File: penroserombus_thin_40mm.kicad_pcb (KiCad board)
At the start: 2 copper layers, 72.4 x 23.5 mm, 15 parts, among them J1 Conn_01x03_Female, J2 Conn_01x03_Female, J3 Conn_01x03_Male, J4 Conn_01x03_Male, M2 MountingHole_2.2mm_M2_ISO7380, SW1 SW_DPDT_x2

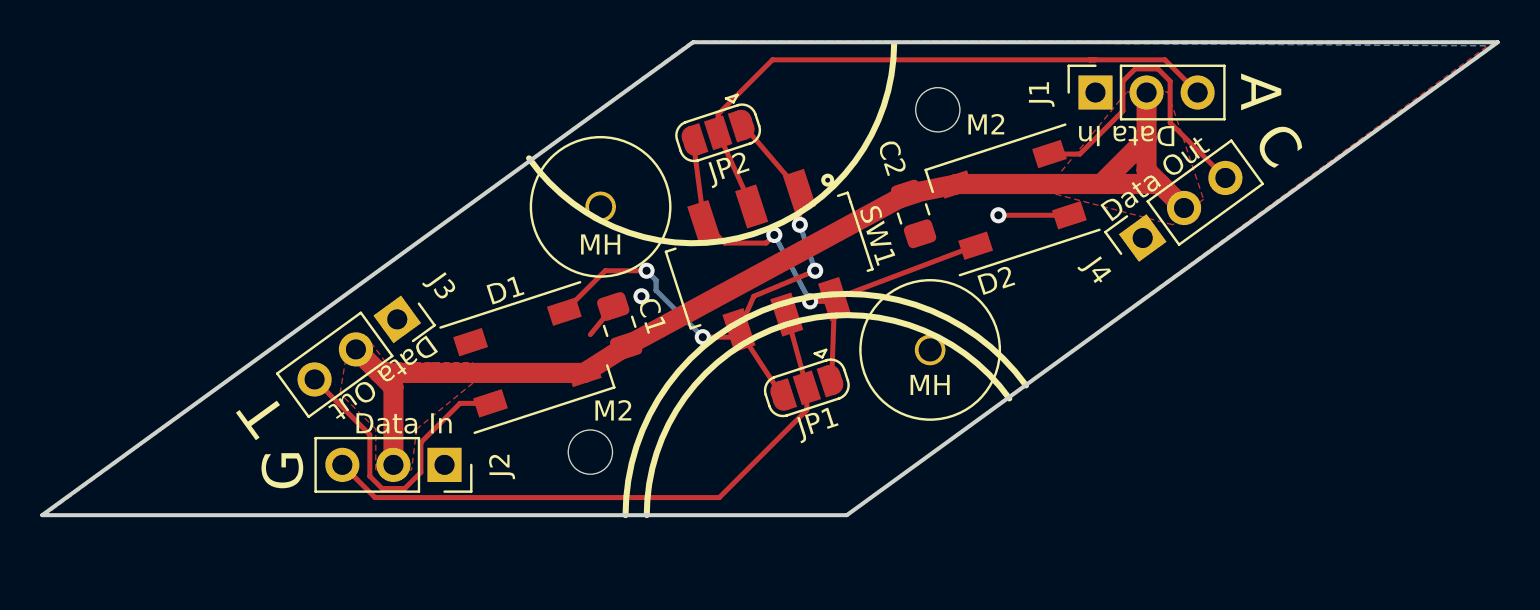
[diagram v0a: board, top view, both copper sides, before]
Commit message: made 3535 led version
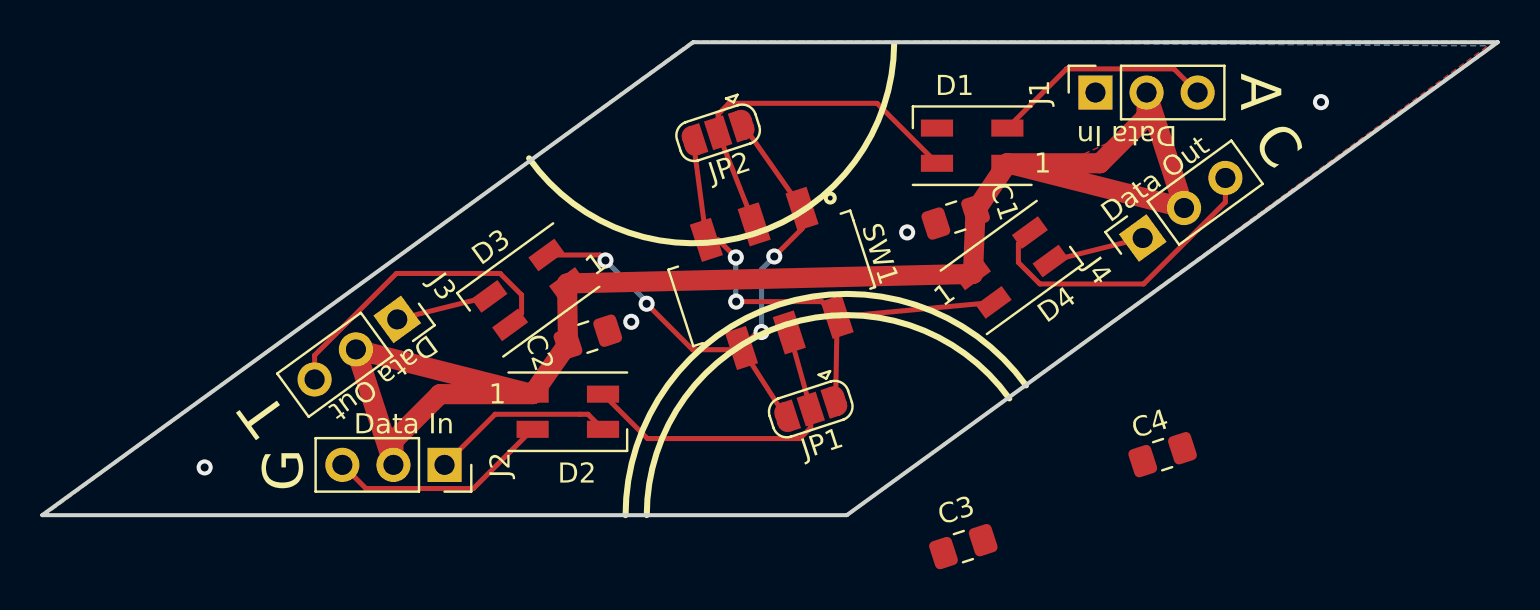
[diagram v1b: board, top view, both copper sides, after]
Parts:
- removed M2 (x2): MountingHole_2.2mm_M2_ISO7380, MountingHole:MountingHole_2.2mm_M2_ISO7380
- removed MH (x2): Pushpin_mountinghole, penroserombus:Pushpin_mountinghole
- added C3: C, Capacitor_SMD:C_0805_2012Metric_Pad1.18x1.45mm_HandSolder, F.Cu at (164.6, 86.6)
- added C4: C, Capacitor_SMD:C_0805_2012Metric_Pad1.18x1.45mm_HandSolder, F.Cu at (174.5, 82.0)
- added D3: SK6812, LED_SMD:LED_SK6812MINI_PLCC4_3.5x3.5mm_P1.75mm, F.Cu at (143.0, 73.9)
- added D4: SK6812, LED_SMD:LED_SK6812MINI_PLCC4_3.5x3.5mm_P1.75mm, F.Cu at (167.0, 72.7)
- D1, D2: footprint LED_SMD:LED_SK6812_PLCC4_5.0x5.0mm_P3.2mm -> LED_SMD:LED_SK6812MINI_PLCC4_3.5x3.5mm_P1.75mm
- moved D2 24.5 mm to (144.9, 79.9), turned to 0 degrees
- moved D1 24.5 mm to (165.0, 66.7), turned to 180 degrees
- moved C1 17.6 mm to (164.2, 70.2), turned to 18 degrees
- moved C2 17.3 mm to (145.9, 76.2), turned to 198 degrees
- moved JP1 1.08 mm to (157.0, 79.8)
- moved SW1 0.90 mm to (155.1, 73.3)
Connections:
- J1 pad 3: Net-(J1-Pad3) -> Net-(D1-Pad2)
- J2 pad 3: Net-(J2-Pad3) -> Net-(D2-Pad2)
- J3 pad 3: Net-(D1-Pad4) -> Net-(D3-Pad4)
- J4 pad 3: Net-(D2-Pad4) -> Net-(D4-Pad4)
- JP1 pad 1: Net-(D2-Pad2) -> Net-(D4-Pad2)
- JP1 pad 2: Net-(J2-Pad3) -> Net-(D2-Pad4)
- JP1 pad 3: Net-(D1-Pad2) -> Net-(D3-Pad2)
- JP2 pad 1: Net-(D1-Pad2) -> Net-(D3-Pad2)
- JP2 pad 2: Net-(J1-Pad3) -> Net-(D1-Pad4)
- JP2 pad 3: Net-(D2-Pad2) -> Net-(D4-Pad2)
- SW1 pad 1: Net-(D1-Pad2) -> Net-(D3-Pad2)
- SW1 pad 2: Net-(J1-Pad3) -> Net-(D1-Pad4)
- SW1 pad 3: Net-(D2-Pad2) -> Net-(D4-Pad2)
- SW1 pad 4: Net-(D2-Pad2) -> Net-(D4-Pad2)
- SW1 pad 5: Net-(J2-Pad3) -> Net-(D2-Pad4)
- SW1 pad 6: Net-(D1-Pad2) -> Net-(D3-Pad2)
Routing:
- net Net-(J1-Pad3): track 30.9 -> 0.00 mm
- net Net-(J2-Pad3): track 30.4 -> 0.00 mm
- net Net-(D3-Pad2): track 0.00 -> 29.2 mm, vias 0 -> 4
- net Net-(D4-Pad2): track 0.00 -> 26.5 mm, vias 0 -> 2
- net VCC: track 57.4 -> 80.6 mm
- net Net-(D1-Pad2): track 29.2 -> 11.2 mm, vias 4 -> 0
- net Net-(D3-Pad4): track 0.00 -> 15.3 mm
- net Net-(D4-Pad4): track 0.00 -> 15.3 mm
- net Net-(D2-Pad2): track 24.9 -> 11.2 mm, vias 2 -> 0
- net GND: track 5.37 -> 18.7 mm, vias 2 -> 4
- net Net-(D1-Pad4): track 14.9 -> 18.2 mm
- net Net-(D2-Pad4): track 14.8 -> 16.3 mm

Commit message: added mounting holes
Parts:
- added MH: Pushpin_mountinghole, penroserombus:Pushpin_mountinghole, F.Cu at (162.7, 78.0)
- added MH: Pushpin_mountinghole, penroserombus:Pushpin_mountinghole, F.Cu at (147.3, 68.7)
- moved C3 16.4 mm to (179.7, 80.4), turned to 90 degrees
- moved C4 9.52 mm to (183.9, 80.5), turned to 108 degrees
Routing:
- net GND: track 18.7 -> 14.0 mm
- net Net-(D3-Pad2): track 29.2 -> 29.4 mm, vias 4 -> 3
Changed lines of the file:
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@@
     (thickness 1.6)
     (drawings 31)
-    (tracks 84)
+    (tracks 80)
     (zones 0)
-    (modules 15)
+    (modules 17)
     (nets 11)
   )
@@
     (mod_text_size 1 1)
     (mod_text_width 0.15)
-    (pad_size 1.524 1.524)
-    (pad_drill 1.1)
+    (pad_size 1.15 1.15)
+    (pad_drill 1.15)
     (pad_to_mask_clearance 0)
     (aux_axis_origin 0 0)
@@
     (add_net VCC)
   )
+  (module penroserombus:Pushpin_mountinghole (layer F.Cu)
+    (at 162.687 77.978)
+    (fp_text reference MH (at 0.1 -1.5) (layer F.SilkS)
+      (effects (font (size 1 1) (thickness 0.15)))
+    )
+    (fp_text value Pushpin_mountinghole (at -0.1 -5.1) (layer F.Fab)
+      (effects (font (size 1 1) (thickness 0.15)))
+    )
+    (fp_circle (center 0 0) (end 4 0) (layer F.CrtYd) (width 0.12))
+    (fp_circle (center 0 0) (end 2.4 -2.5) (layer F.SilkS) (width 0.12))
+    (pad "" np_thru_hole circle (at 0 0) (size 1.15 1.15) (drill 1.15) (layers *.Cu *.Mask))
+  )
+  (module penroserombus:Pushpin_mountinghole (layer F.Cu)
+    (at 147.32 68.707)
+    (fp_text reference MH (at 0.1 -1.5) (layer F.SilkS)
+      (effects (font (size 1 1) (thickness 0.15)))
+    )
+    (fp_text value Pushpin_mountinghole (at -0.1 -5.1) (layer F.Fab)
+      (effects (font (size 1 1) (thickness 0.15)))
+    )
+    (fp_circle (center 0 0) (end 4 0) (layer F.CrtYd) (width 0.12))
+    (fp_circle (center 0 0) (end 2.4 -2.5) (layer F.SilkS) (width 0.12))
+    (pad "" np_thru_hole circle (at 0 0) (size 1.15 1.15) (drill 1.15) (layers *.Cu *.Mask))
+  )
   (module Capacitor_SMD:C_0805_2012Metric_Pad1.18x1.45mm_HandSolder (layer F.Cu)
-    (at 164.592 86.614 18)
+    (at 179.705 80.3695 90)
     (descr "Capacitor SMD 0805 (2012 Metric), square (rectangular) end terminal, IPC_7351 nominal with elongated pad for handsoldering. (Body size source: IPC-SM-782 page 76, https://www.pcb-3d.com/wordpress/wp-content/uploads/ipc-sm-782a_amendment_1_and_2.pdf, https://docs.google.com/spreadsheets/d/1BsfQQcO9C6DZCsRaXUlFlo91Tg2WpOkGARC1WS5S8t0/edit?usp=sharing), generated with kicad-footprint-generator")
     (tags "capacitor handsolder")
     (attr smd)
-    (fp_text reference C3 (at 0.213381 -1.819148 198) (layer F.SilkS)
-      (effects (font (size 1 1) (thickness 0.15)))
-    )
-    (fp_text value C (at 0 1.68 18) (layer F.Fab)
+    (fp_text reference C3 (at 1.397 -1.524 270) (layer F.SilkS)
+      (effects (font (size 1 1) (thickness 0.15)))
+    )
+    (fp_text value C (at 0 1.68 90) (layer F.Fab)
       (effects (font (size 1 1) (thickness 0.15)))
     )
@@
     (fp_line (start -1 -0.625) (end 1 -0.625) (layer F.Fab) (width 0.1))
     (fp_line (start -1 0.625) (end -1 -0.625) (layer F.Fab) (width 0.1))
-    (fp_text user %R (at 0 0 18) (layer F.Fab)
+    (fp_text user %R (at 0 0 90) (layer F.Fab)
       (effects (font (size 0.5 0.5) (thickness 0.08)))
     )
-    (pad 2 smd roundrect (at 1.0375 0 18) (size 1.175 1.45) (layers F.Cu F.Paste F.Mask) (roundrect_rratio 0.212766)
-      (net 1 VCC))
-    (pad 1 smd roundrect (at -1.0375 0 18) (size 1.175 1.45) (layers F.Cu F.Paste F.Mask) (roundrect_rratio 0.212766)
+    (pad 2 smd roundrect (at 1.0375 0 90) (size 1.175 1.45) (layers F.Cu F.Paste F.Mask) (roundrect_rratio 0.212766)
+      (net 1 VCC))
+    (pad 1 smd roundrect (at -1.0375 0 90) (size 1.175 1.45) (layers F.Cu F.Paste F.Mask) (roundrect_rratio 0.212766)
       (net 2 GND))
     (model ${KISYS3DMOD}/Capacitor_SMD.3dshapes/C_0805_2012Metric.wrl
@@
   )
   (module Capacitor_SMD:C_0805_2012Metric_Pad1.18x1.45mm_HandSolder (layer F.Cu)
-    (at 174.498 82.042 18)
+    (at 183.896 80.518 108)
     (descr "Capacitor SMD 0805 (2012 Metric), square (rectangular) end terminal, IPC_7351 nominal with elongated pad for handsoldering. (Body size source: IPC-SM-782 page 76, https://www.pcb-3d.com/wordpress/wp-content/uploads/ipc-sm-782a_amendment_1_and_2.pdf, https://docs.google.com/spreadsheets/d/1BsfQQcO9C6DZCsRaXUlFlo91Tg2WpOkGARC1WS5S8t0/edit?usp=sharing), generated with kicad-footprint-generator")
     (tags "capacitor handsolder")
     (attr smd)
-    (fp_text reference C4 (at -0.126092 -1.646178 198) (layer F.SilkS)
-      (effects (font (size 1 1) (thickness 0.15)))
-    )
-    (fp_text value C (at 0 1.68 18) (layer F.Fab)
+    (fp_text reference C4 (at -0.126092 -1.646178 288) (layer F.SilkS)
+      (effects (font (size 1 1) (thickness 0.15)))
+    )
+    (fp_text value C (at 0 1.68 108) (layer F.Fab)
       (effects (font (size 1 1) (thickness 0.15)))
     )
@@
     (fp_line (start 1.88 -0.98) (end 1.88 0.98) (layer F.CrtYd) (width 0.05))
     (fp_line (start 1.88 0.98) (end -1.88 0.98) (layer F.CrtYd) (width 0.05))
-    (fp_text user %R (at 0 0 18) (layer F.Fab)
+    (fp_text user %R (at 0 0 108) (layer F.Fab)
       (effects (font (size 0.5 0.5) (thickness 0.08)))
     )
-    (pad 1 smd roundrect (at -1.0375 0 18) (size 1.175 1.45) (layers F.Cu F.Paste F.Mask) (roundrect_rratio 0.212766)
-      (net 2 GND))
-    (pad 2 smd roundrect (at 1.0375 0 18) (size 1.175 1.45) (layers F.Cu F.Paste F.Mask) (roundrect_rratio 0.212766)
+    (pad 1 smd roundrect (at -1.0375 0 108) (size 1.175 1.45) (layers F.Cu F.Paste F.Mask) (roundrect_rratio 0.212766)
+      (net 2 GND))
+    (pad 2 smd roundrect (at 1.0375 0 108) (size 1.175 1.45) (layers F.Cu F.Paste F.Mask) (roundrect_rratio 0.212766)
       (net 1 VCC))
     (model ${KISYS3DMOD}/Capacitor_SMD.3dshapes/C_0805_2012Metric.wrl
@@
   (via (at 182.372 64.516) (size 0.8) (drill 0.4) (layers F.Cu B.Cu) (net 2))
   (via (at 126.873 82.677) (size 0.8) (drill 0.4) (layers F.Cu B.Cu) (net 2))
-  (segment (start 136.448848 75.316838) (end 141.029805 74.17308) (width 0.25) (layer F.Cu) (net 2))
   (segment (start 145.927399 80.032699) (end 146.6774 80.7827) (width 0.25) (layer F.Cu) (net 2))
   (segment (start 138.799045 82.55) (end 141.316346 80.032699) (width 0.25) (layer F.Cu) (net 2))
@@
   (segment (start 155.769254 80.178444) (end 153.562332 76.738277) (width 0.25) (layer F.Cu) (net 8))
   (segment (start 153.636373 65.638278) (end 156.571668 69.819723) (width 0.25) (layer F.Cu) (net 8))
-  (via (at 146.799966 72.386382) (size 0.8) (drill 0.4) (layers F.Cu B.Cu) (net 8))
-  (segment (start 146.529416 72.115832) (end 146.799966 72.386382) (width 0.25) (layer F.Cu) (net 8))
-  (segment (start 143.861365 72.115832) (end 146.529416 72.115832) (width 0.25) (layer F.Cu) (net 8))
-  (via (at 148.846748 74.538847) (size 0.8) (drill 0.4) (layers F.Cu B.Cu) (net 8))
-  (segment (start 148.846748 74.433164) (end 148.846748 74.538847) (width 0.25) (layer B.Cu) (net 8))
-  (segment (start 146.799966 72.386382) (end 148.846748 74.433164) (width 0.25) (layer B.Cu) (net 8))
-  (segment (start 148.846748 74.538847) (end 151.13 76.822099) (width 0.25) (layer F.Cu) (net 8))
-  (segment (start 153.47851 76.822099) (end 153.562332 76.738277) (width 0.25) (layer F.Cu) (net 8))
-  (segment (start 151.13 76.822099) (end 153.47851 76.822099) (width 0.25) (layer F.Cu) (net 8))
   (via (at 155.192259 72.188983) (size 0.8) (drill 0.4) (layers F.Cu B.Cu) (net 8))
   (segment (start 156.571668 70.809574) (end 155.192259 72.188983) (width 0.25) (layer F.Cu) (net 8))
@@
   (segment (start 154.354609 75.946) (end 153.562332 76.738277) (width 0.25) (layer F.Cu) (net 8))
   (segment (start 154.559 75.946) (end 154.354609 75.946) (width 0.25) (layer F.Cu) (net 8))
+  (via (at 150.622 72.136) (size 0.8) (drill 0.4) (layers F.Cu B.Cu) (net 8))
+  (segment (start 150.601832 72.115832) (end 150.622 72.136) (width 0.25) (layer F.Cu) (net 8))
+  (segment (start 143.861365 72.115832) (end 150.601832 72.115832) (width 0.25) (layer F.Cu) (net 8))
+  (segment (start 154.512252 71.508976) (end 155.192259 72.188983) (width 0.25) (layer B.Cu) (net 8))
+  (segment (start 151.249024 71.508976) (end 154.512252 71.508976) (width 0.25) (layer B.Cu) (net 8))
+  (segment (start 150.622 72.136) (end 151.249024 71.508976) (width 0.25) (layer B.Cu) (net 8))
   (segment (start 158.072806 74.422) (end 158.190614 74.304192) (width 0.25) (layer F.Cu) (net 9) (status 30))
   (segment (start 158.242 79.375) (end 158.317614 75.193192) (width 0.25) (layer F.Cu) (net 9))

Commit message: updated gerbers
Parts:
- removed C3, C4: C, Capacitor_SMD:C_0805_2012Metric_Pad1.18x1.45mm_HandSolder
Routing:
- net Net-(D3-Pad2): track 29.4 -> 36.1 mm, vias 3 -> 2
- net Net-(D4-Pad2): track 26.5 -> 27.1 mm
- net GND: vias 4 -> 8
